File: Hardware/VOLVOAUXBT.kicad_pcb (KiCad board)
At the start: 2 copper layers, 110 x 30 mm, 62 parts, among them J1 10118193-0001LF, J10 Conn_01x02_Pin, J11 Conn_01x02_Pin, J14 Conn_01x05_Pin, J15 Conn_01x02_Pin, J16 Conn_01x02_Pin, J17 Conn_01x01_Pin, J18 Conn_01x02_Pin, J19 Conn_01x01_Pin, J2 10118193-0001LF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

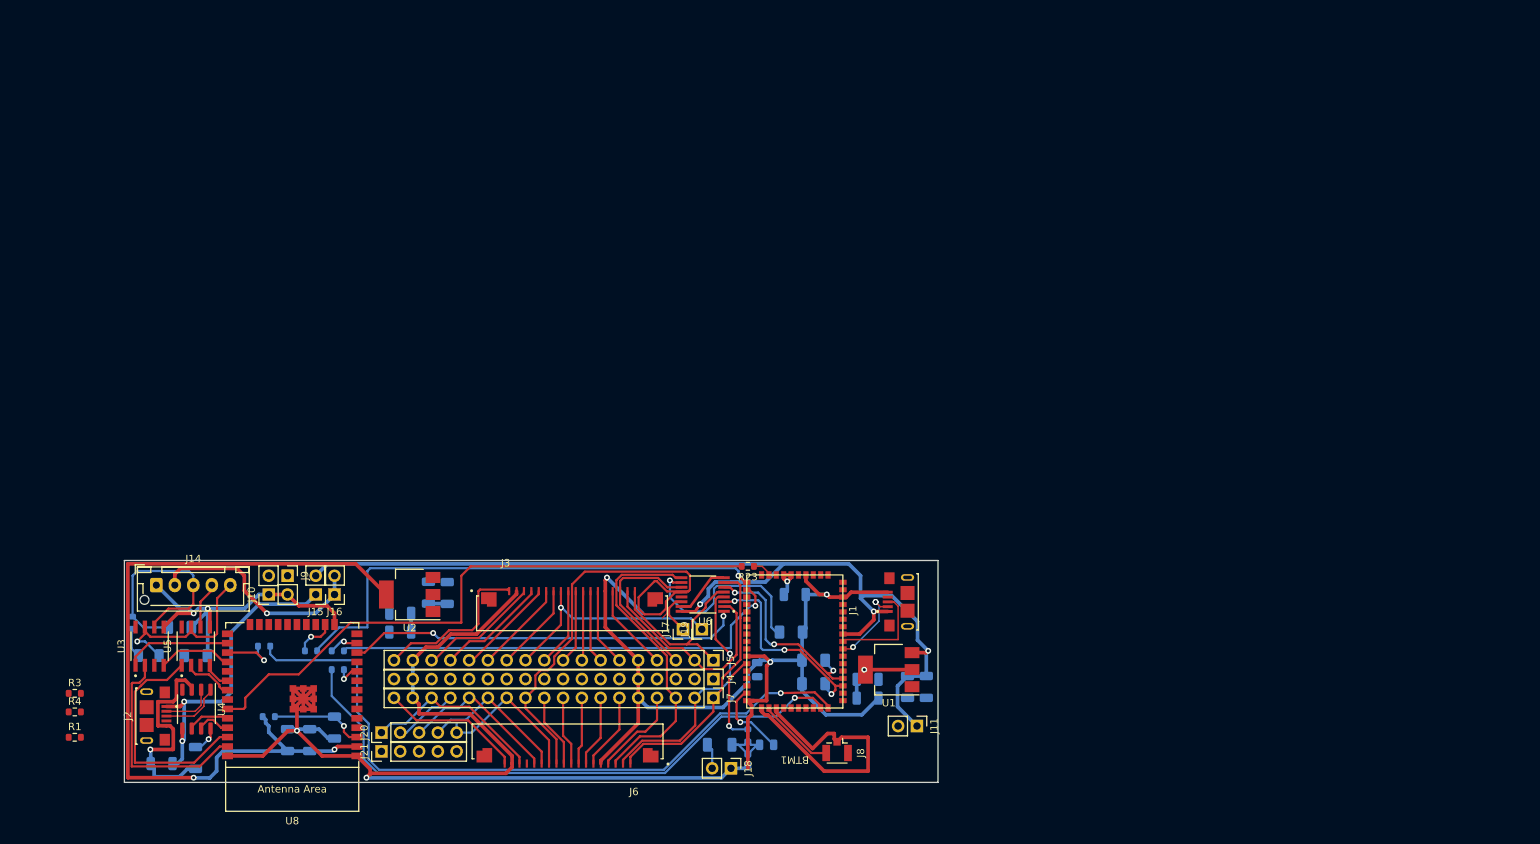
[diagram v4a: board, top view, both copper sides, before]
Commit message: Routing with low side clearence. Pending accurate measurments for produciton
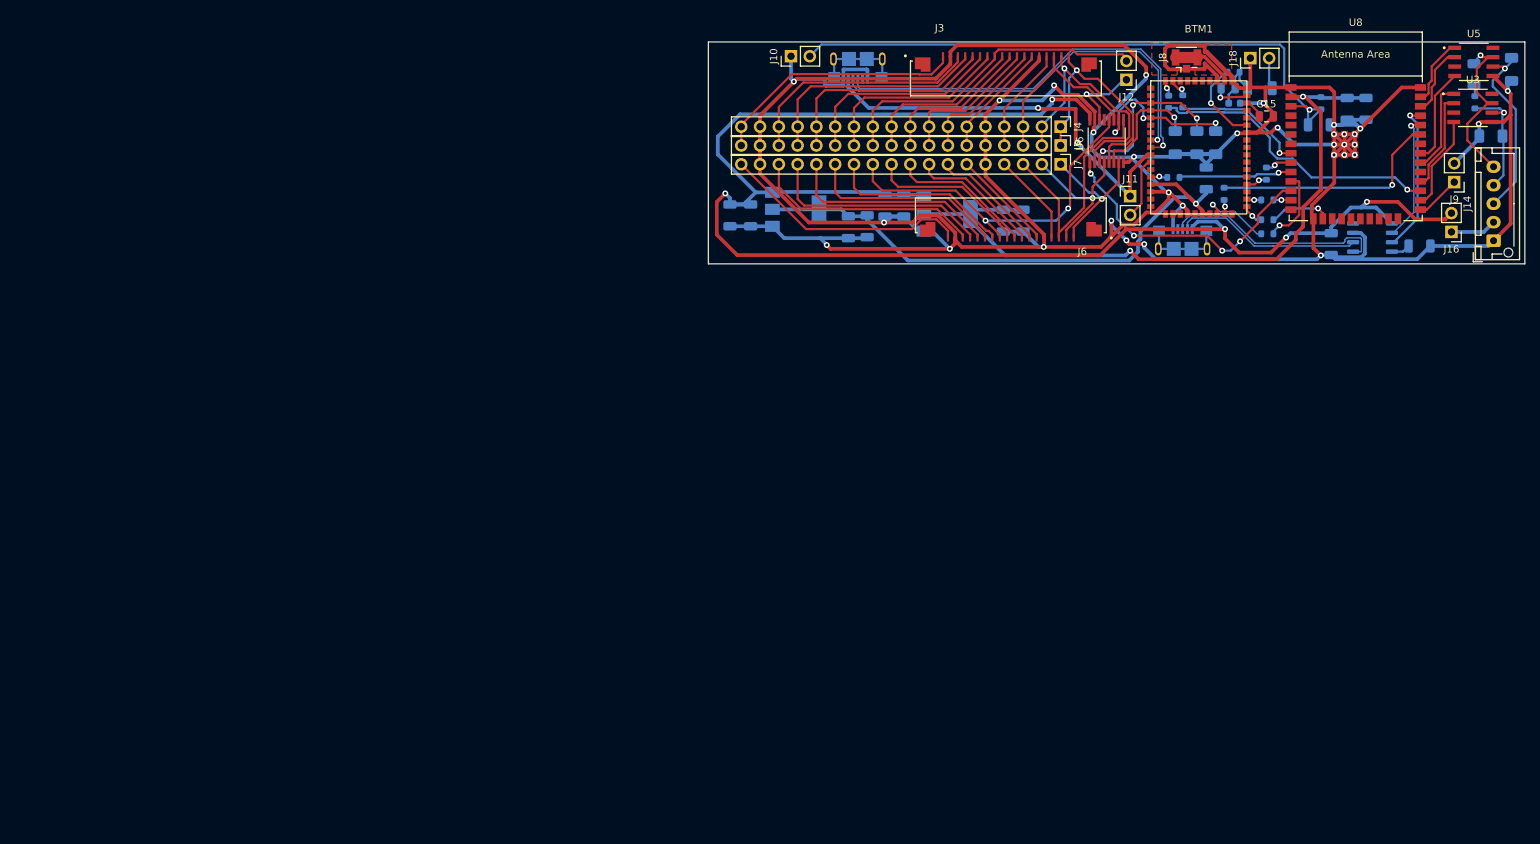
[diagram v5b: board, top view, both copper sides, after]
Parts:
- removed J15: Conn_01x02_Pin, Connector_PinHeader_2.54mm:PinHeader_1x02_P2.54mm_Vertical
- removed J17, J19: Conn_01x01_Pin, Connector_PinHeader_2.54mm:PinHeader_1x01_P2.54mm_Vertical
- removed J20, J21: Conn_01x05_Pin, Connector_PinHeader_2.54mm:PinHeader_1x05_P2.54mm_Vertical
- added J12: Conn_01x02_Pin, Connector_PinHeader_2.54mm:PinHeader_1x02_P2.54mm_Vertical, F.Cu at (188.3, 57.4)
- C15: moved to F.Cu
- J1, J2, R1, R23, R3, R4, U1, U2, U4: moved to B.Cu
- moved D1 195.6 mm to (235.3, 56.6), turned to 90 degrees
- moved C18 194.7 mm to (240.4, 56.0), turned to -90 degrees
- moved R2 194.6 mm to (235.5, 60.5), turned to -90 degrees
- moved U3 193.1 mm to (235.2, 61.2), turned to 0 degrees
- moved U5 190.0 mm to (235.3, 55.0), turned to 0 degrees
- moved C16 189.3 mm to (237.6, 65.0), turned to 180 degrees
- moved J14 186.7 mm to (238.0, 79.2), turned to 90 degrees
- moved C11 179.4 mm to (228.0, 79.9), turned to 0 degrees
- moved R4 176.8 mm to (207.3, 70.1), turned to 90 degrees
- moved R1 175.0 mm to (207.4, 78.2)
- moved C10 173.0 mm to (216.0, 79.6), turned to 90 degrees
- moved U4 171.3 mm to (221.6, 78.7), turned to 0 degrees
- moved R3 169.8 mm to (196.0, 60.3), turned to -90 degrees
- moved C25 166.8 mm to (218.2, 61.3), turned to -90 degrees
- moved J9 166.5 mm to (232.7, 71.2), turned to 180 degrees
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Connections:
- C1 pad 1: BTM_USB_VBUS -> VBUS
- C2 pad 1: BTM_USB_VBUS -> VBUS
- C23 pad 1: Net-(U8-EN/CHIP_PU) -> /ESP_RST
- J10 pad 2: GND -> /ESP_RST
- J14 pad 3: /LIN1 -> /LIN2
- J14 pad 4: /LIN2 -> /LIN1
- J16 pad 2: /EXT_5V -> VBUS
- J9 pad 1: /ESP_RST -> /GPIO0
- J9 pad 2: /GPIO0 -> GND
- R16 pad 2: Net-(U8-EN/CHIP_PU) -> /ESP_RST
- R20 pad 1: /BTM_NEXT -> /BTM_ON/OFF
- R3 pad 1: /BTM_ON/OFF -> /BTM_NEXT
- U1 pad 3: BTM_USB_VBUS -> VBUS
- U6 pad 16: BTM_USB_VBUS -> VBUS
- U8 pad 26: /LIN1_RXD -> /LIN1_TXD
- U8 pad 28: /LIN1_TXD -> /LIN1_SLP
- U8 pad 3: Net-(U8-EN/CHIP_PU) -> /ESP_RST
- U8 pad 30: /LIN2_TXD -> /LIN1_RXD
- U8 pad 31: /LIN2_SLP -> /LIN2_TXD
- U8 pad 36: /LIN2_RXD -> /LIN2_SLP
- U8 pad 37: /LIN1_SLP -> /LIN2_RXD
- U8 pad 4: Net-(J21-Pin_2) -> unconnected-(U8-SENSOR_VP/GPIO36/ADC1_CH0-Pad4)
- U8 pad 5: Net-(J21-Pin_1) -> unconnected-(U8-SENSOR_VN/GPIO39/ADC1_CH3-Pad5)
- U8 pad 6: Net-(J21-Pin_4) -> unconnected-(U8-GPIO34/ADC1_CH6-Pad6)
- U8 pad 7: Net-(J21-Pin_3) -> unconnected-(U8-GPIO35/ADC1_CH7-Pad7)
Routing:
- net VBUS: track 42.7 -> 222.0 mm, vias 2 -> 5
- net GND: track 429.6 -> 568.5 mm, vias 8 -> 32
- net /BTM_PREVIOUS: track 95.5 -> 2.38 mm
- net /ESP_RST: track 0.00 -> 84.0 mm, vias 0 -> 1
- net BTM_USB_VBUS: track 136.2 -> 55.1 mm, vias 3 -> 2
- net /BTM_NEXT: track 81.7 -> 2.75 mm
- net /BTM_GPIO_R2: track 68.5 -> 2.99 mm
- net BTM_3V3: track 16.2 -> 78.4 mm, vias 2 -> 1
- net /BTM_GPIO_R1: track 62.8 -> 2.12 mm
- net Net-(U8-GPIO21): track 82.2 -> 31.9 mm, vias 0 -> 1
- net /BTM_USB_DN: track 11.1 -> 56.1 mm, vias 3 -> 1
- net /BTM_USB_DP: track 13.7 -> 57.8 mm, vias 0 -> 1
- net Net-(U8-GPIO16): track 7.62 -> 40.1 mm
- net /EXT_5V: track 30.7 -> 6.24 mm, vias 1 -> 0
- net /USB_DP: track 8.23 -> 30.4 mm
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- added copper zone on F.Cu, net GND
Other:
- board size 110 x 30 mm -> 110.4 x 30 mm
- board text added: "5.9"
- board text added: "6.35"

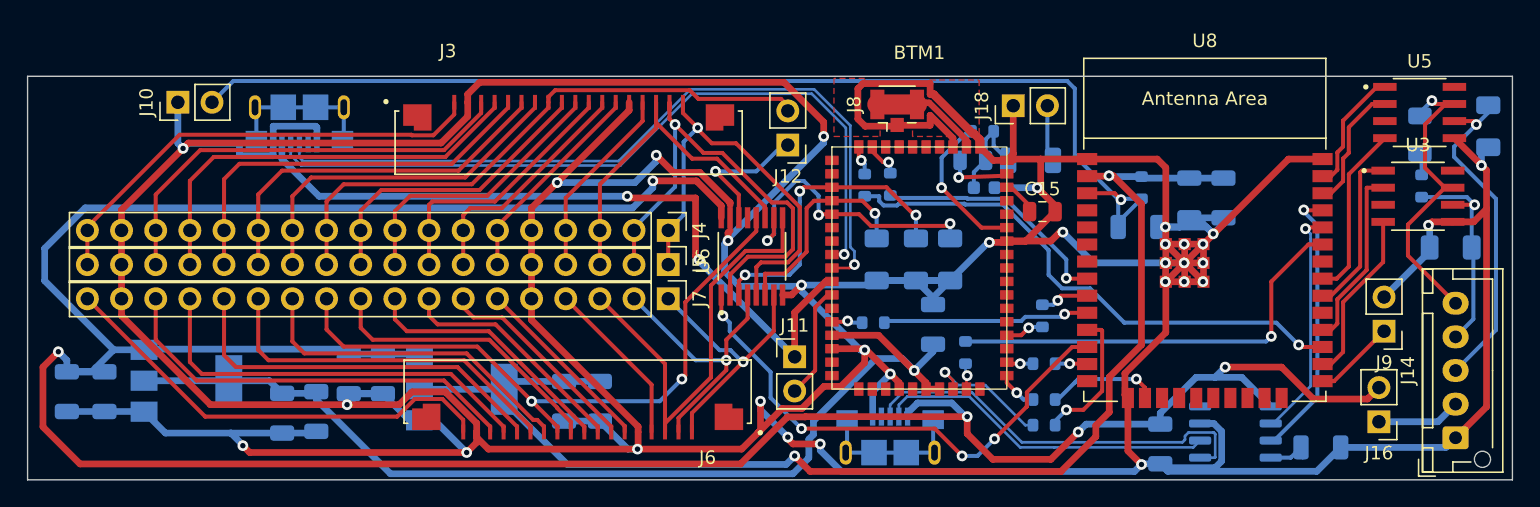
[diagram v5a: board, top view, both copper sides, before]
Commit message: XST set to 2.5mm. Swapping for 2.54mm
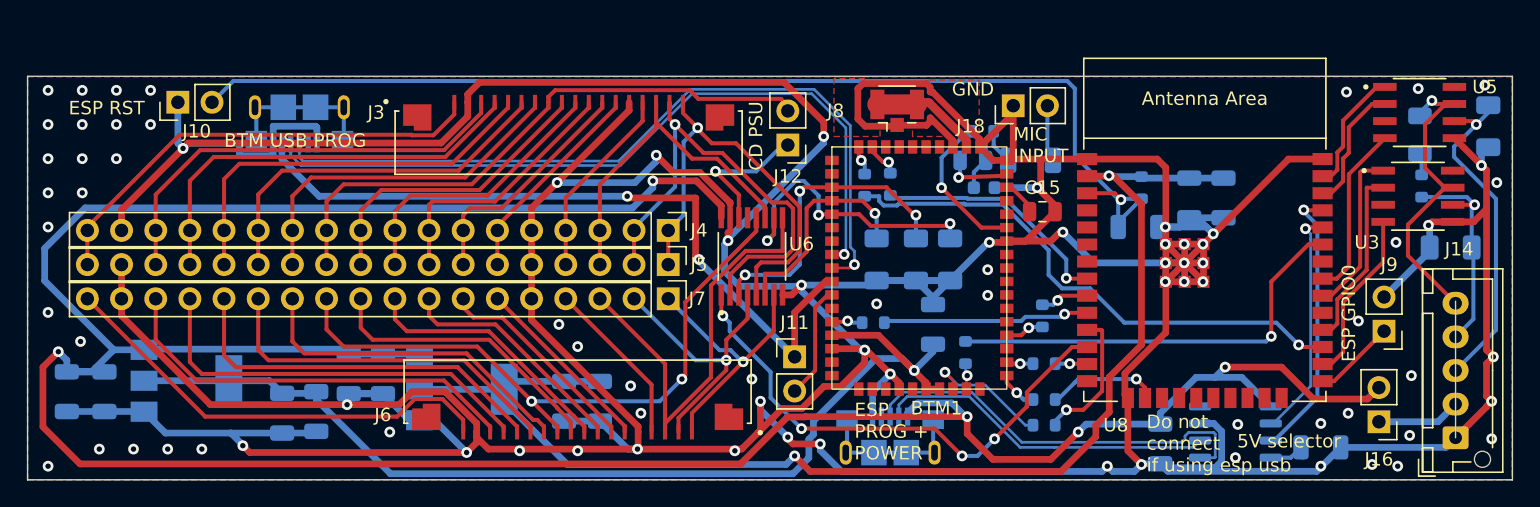
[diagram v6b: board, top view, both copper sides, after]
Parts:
- C16: value C -> 1nF
- C18: value C -> 220pF
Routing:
- net GND: track 568.5 -> 570.6 mm, vias 32 -> 84
- added copper zone on B.Cu, net GND
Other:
- outline, holes or cut-outs redrawn
- board text added: "5V selector"
- board text added: "BTM USB PROG"
- board text added: "CD PSU"
- board text added: "Do not connect if using esp usb"
- board text added: "ESP GPIO0"
- board text added: "ESP PROG + POWER"
- board text added: "ESP RST"
- board text added: "GND"
- board text added: "MIC INPUT"
